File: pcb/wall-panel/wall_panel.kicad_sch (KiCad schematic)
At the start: 0 parts

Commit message: wall panel v0.3
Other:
- sheet CM4_HighSpeed ports: added BACKLIGHT_POWER; removed none
- sheet Power Filtering ports: added BACKLIGHT_POWER; removed none
- company: Grigorii Merkushev (aka brushknight) -> dotstar.tech
- title: Wall panel -> Wall Panel
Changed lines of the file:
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@@
 	(paper "A3")
 	(title_block
-		(title "Wall panel")
-		(date "2026-01-09")
-		(rev "1")
-		(company "Grigorii Merkushev (aka brushknight)")
-		(comment 1 "brushknight.com")
+		(title "Wall Panel")
+		(date "2026-02-02")
+		(rev "v0.3")
+		(company "dotstar.tech")
+		(comment 1 "designed by Grigorii Merkushev (aka brushknight)")
+		(comment 2 "brushknight.com")
 	)
 	(text "Connectors\n-------\nFAN\nBattery"
@@
 	(wire
 		(pts
+			(xy 168.91 87.63) (xy 203.2 87.63)
+		)
+		(stroke
+			(width 0)
+			(type default)
+		)
+	)
+	(wire
+		(pts
 			(xy 137.16 101.6) (xy 137.16 106.68)
 		)
@@
 	(wire
 		(pts
+			(xy 203.2 46.99) (xy 218.44 46.99)
+		)
+		(stroke
+			(width 0)
+			(type default)
+		)
+	)
+	(wire
+		(pts
 			(xy 168.91 135.89) (xy 179.07 135.89)
 		)
@@
 			(width 0)
 			(type solid)
+		)
+	)
+	(wire
+		(pts
+			(xy 203.2 87.63) (xy 203.2 46.99)
+		)
+		(stroke
+			(width 0)
+			(type default)
 		)
 	)
@@
 		(pin "TOUCH_SDA" input
 			(at 168.91 44.45 0)
+			(effects
+				(font
+					(size 1.27 1.27)
+				)
+				(justify right)
+			)
+		)
+		(pin "BACKLIGHT_POWER" input
+			(at 168.91 87.63 0)
 			(effects
 				(font
@@
 			(effects
 				(font
+					(size 1.27 1.27)
+				)
+				(justify left)
+			)
+		)
+		(pin "BACKLIGHT_POWER" output
+			(at 218.44 46.99 180)
+			(effects
+				(font

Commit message: small fixes of v0.3.1
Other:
- sheet CM4_GPIO ( Ethernet, GPIO, SDCARD) ports: added DISPLAY_PWM; removed none
- sheet CM4_HighSpeed ports: added DISPLAY_PWM; removed none
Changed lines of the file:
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@@
 	(title_block
 		(title "Wall Panel")
-		(date "2026-02-02")
-		(rev "v0.3")
+		(date "2026-02-25")
+		(rev "v0.3.1")
 		(company "dotstar.tech")
 		(comment 1 "designed by Grigorii Merkushev (aka brushknight)")
@@
 	(wire
 		(pts
+			(xy 180.34 128.27) (xy 180.34 90.17)
+		)
+		(stroke
+			(width 0)
+			(type default)
+		)
+	)
+	(wire
+		(pts
 			(xy 105.41 110.49) (xy 140.97 110.49)
 		)
@@
 	(wire
 		(pts
+			(xy 168.91 128.27) (xy 180.34 128.27)
+		)
+		(stroke
+			(width 0)
+			(type default)
+		)
+	)
+	(wire
+		(pts
 			(xy 105.41 106.68) (xy 137.16 106.68)
 		)
@@
 			(width 0)
 			(type solid)
+		)
+	)
+	(wire
+		(pts
+			(xy 180.34 90.17) (xy 168.91 90.17)
+		)
+		(stroke
+			(width 0)
+			(type default)
 		)
 	)
@@
 			)
 		)
+		(pin "DISPLAY_PWM" output
+			(at 168.91 128.27 0)
+			(effects
+				(font
+					(size 1.27 1.27)
+				)
+				(justify right)
+			)
+		)
 		(instances
 			(project "wall_panel"
@@
 			(effects
 				(font
+					(size 1.27 1.27)
+				)
+				(justify right)
+			)
+		)
+		(pin "DISPLAY_PWM" input
+			(at 168.91 90.17 0)
+			(effects
+				(font

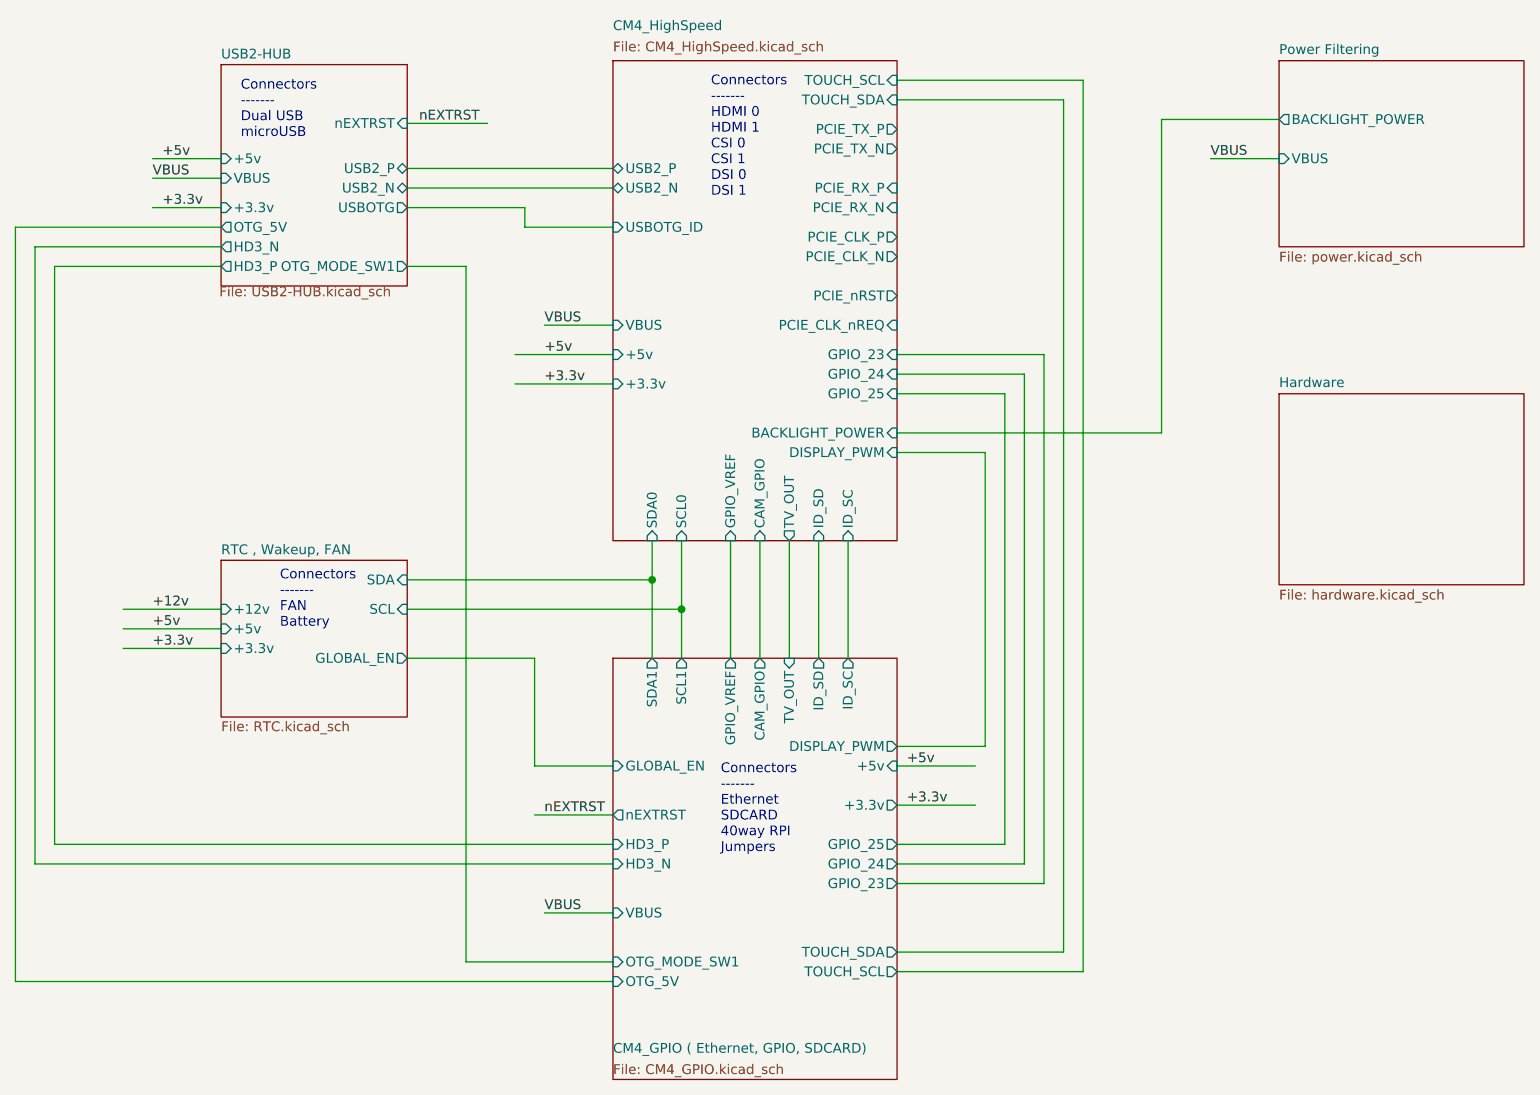
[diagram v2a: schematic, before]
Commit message: pogo pins wall panel
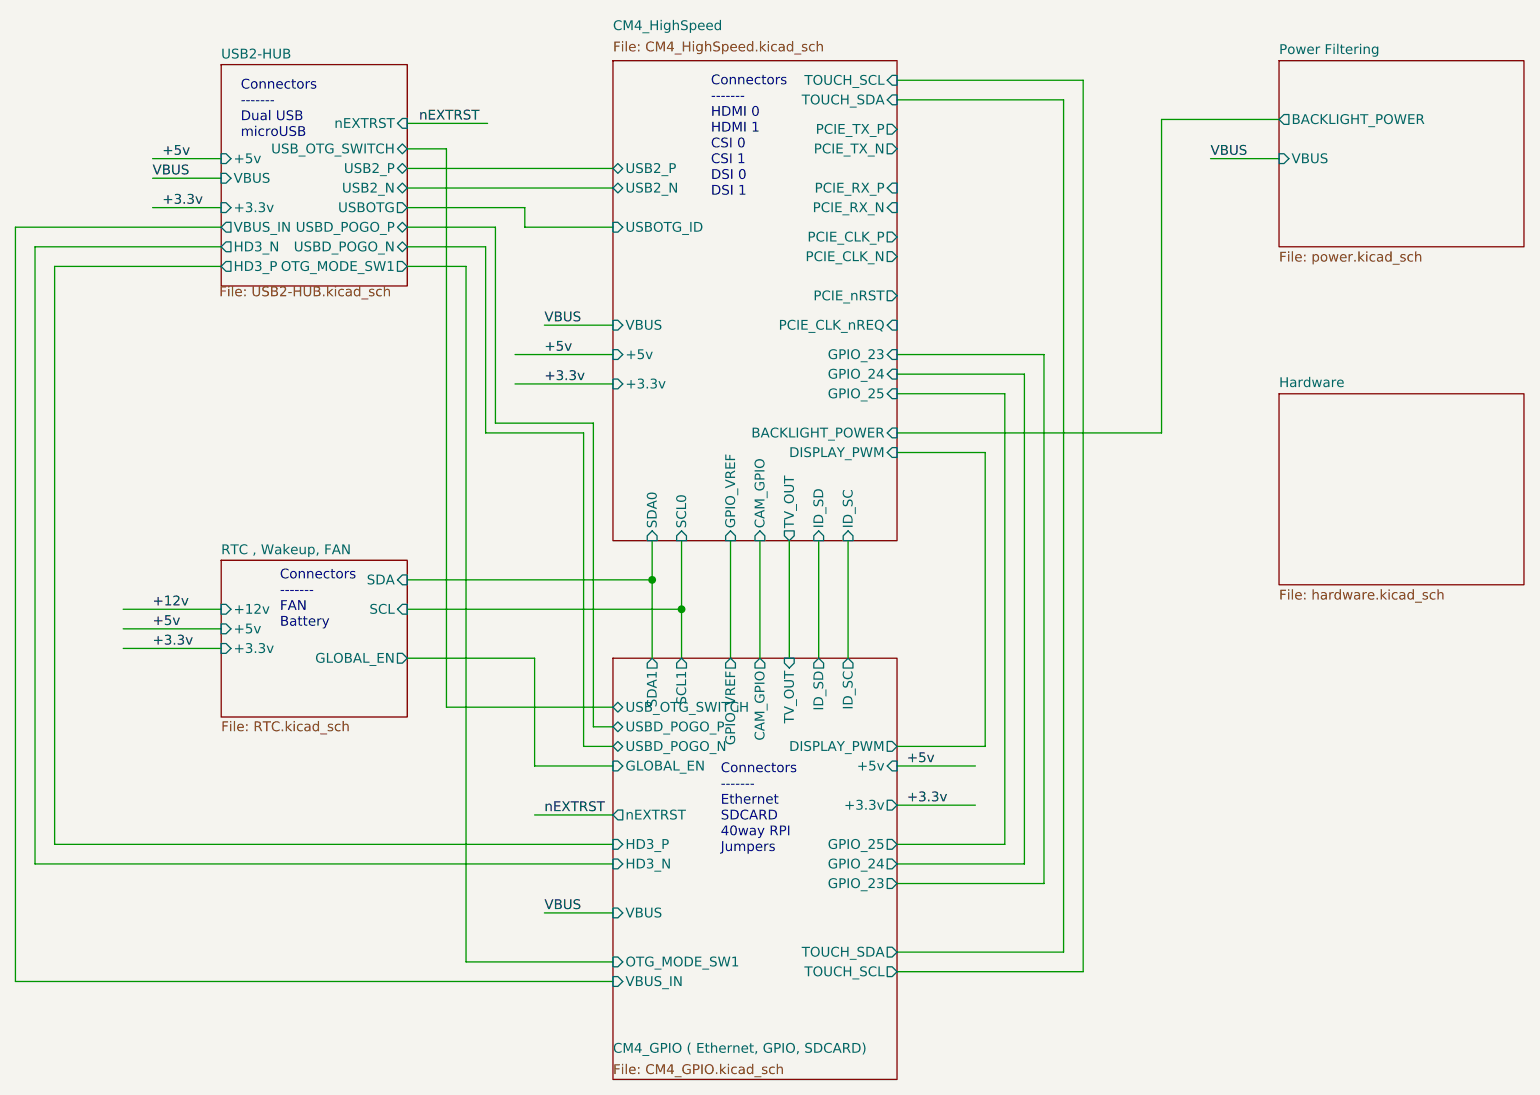
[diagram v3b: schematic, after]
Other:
- sheet CM4_GPIO ( Ethernet, GPIO, SDCARD) ports: added USBD_POGO_N, USBD_POGO_P, USB_OTG_SWITCH, VBUS_IN; removed OTG_5V
- sheet USB2-HUB ports: added USBD_POGO_N, USBD_POGO_P, USB_OTG_SWITCH, VBUS_IN; removed OTG_5V
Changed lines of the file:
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@@
 (kicad_sch
-	(version 20250114)
+	(version 20260306)
 	(generator "eeschema")
-	(generator_version "9.0")
+	(generator_version "10.0")
 	(paper "A3")
 	(title_block
@@
 	(wire
 		(pts
+			(xy 128.27 128.27) (xy 132.08 128.27)
+		)
+		(stroke
+			(width 0)
+			(type default)
+		)
+	)
+	(wire
+		(pts
 			(xy 168.91 143.51) (xy 185.42 143.51)
 		)
@@
 	(wire
 		(pts
+			(xy 129.54 125.73) (xy 129.54 86.36)
+		)
+		(stroke
+			(width 0)
+			(type default)
+		)
+	)
+	(wire
+		(pts
 			(xy 81.28 66.04) (xy 59.69 66.04)
 		)
@@
 	(wire
 		(pts
+			(xy 105.41 50.8) (xy 110.49 50.8)
+		)
+		(stroke
+			(width 0)
+			(type default)
+		)
+	)
+	(wire
+		(pts
 			(xy 147.32 101.6) (xy 147.32 116.84)
 		)
@@
 	(wire
 		(pts
+			(xy 105.41 63.5) (xy 115.57 63.5)
+		)
+		(stroke
+			(width 0)
+			(type default)
+		)
+	)
+	(wire
+		(pts
 			(xy 168.91 135.89) (xy 179.07 135.89)
 		)
@@
 	(wire
 		(pts
+			(xy 115.57 63.5) (xy 115.57 87.63)
+		)
+		(stroke
+			(width 0)
+			(type default)
+		)
+	)
+	(wire
+		(pts
+			(xy 128.27 87.63) (xy 128.27 128.27)
+		)
+		(stroke
+			(width 0)
+			(type default)
+		)
+	)
+	(wire
+		(pts
+			(xy 110.49 123.19) (xy 132.08 123.19)
+		)
+		(stroke
+			(width 0)
+			(type default)
+		)
+	)
+	(wire
+		(pts
+			(xy 110.49 50.8) (xy 110.49 123.19)
+		)
+		(stroke
+			(width 0)
+			(type default)
+		)
+	)
+	(wire
+		(pts
 			(xy 180.34 128.27) (xy 180.34 90.17)
 		)
@@
 	(wire
 		(pts
+			(xy 115.57 87.63) (xy 128.27 87.63)
+		)
+		(stroke
+			(width 0)
+			(type default)
+		)
+	)
+	(wire
+		(pts
 			(xy 203.2 87.63) (xy 203.2 46.99)
 		)
@@
 	(wire
 		(pts
+			(xy 116.84 86.36) (xy 116.84 60.96)
+		)
+		(stroke
+			(width 0)
+			(type default)
+		)
+	)
+	(wire
+		(pts
+			(xy 132.08 125.73) (xy 129.54 125.73)
+		)
+		(stroke
+			(width 0)
+			(type default)
+		)
+	)
+	(wire
+		(pts
 			(xy 132.08 143.51) (xy 57.15 143.51)
 		)
@@
 	(wire
 		(pts
+			(xy 129.54 86.36) (xy 116.84 86.36)
+		)
+		(stroke
+			(width 0)
+			(type default)
+		)
+	)
+	(wire
+		(pts
 			(xy 105.41 66.04) (xy 113.03 66.04)
 		)
@@
 		(pts
 			(xy 113.03 156.21) (xy 132.08 156.21)
+		)
+		(stroke
+			(width 0)
+			(type default)
+		)
+	)
+	(wire
+		(pts
+			(xy 116.84 60.96) (xy 105.41 60.96)
 		)
 		(stroke
@@
 		)
 		(fill
-			(color 255 255 255 0.0000)
+			(color 255 255 255 0)
 		)
 		(property "Sheetname" "CM4_GPIO ( Ethernet, GPIO, SDCARD)"
 			(at 132.08 168.148 0)
+			(show_name no)
+			(do_not_autoplace no)
 			(effects
 				(font
@@
 		(property "Sheetfile" "CM4_GPIO.kicad_sch"
 			(at 132.08 169.418 0)
+			(show_name no)
+			(do_not_autoplace no)
 			(effects
 				(font
@@
 			)
 		)
-		(pin "OTG_5V" input
+		(pin "VBUS_IN" input
 			(at 132.08 158.75 180)
 			(effects
@@
 				)
 				(justify right)
+			)
+		)
+		(pin "USBD_POGO_N" bidirectional
+			(at 132.08 128.27 180)
+			(effects
+				(font
+					(size 1.27 1.27)
+				)
+				(justify left)
+			)
+		)
+		(pin "USBD_POGO_P" bidirectional
+			(at 132.08 125.73 180)
+			(effects
+				(font
+					(size 1.27 1.27)
+				)
+				(justify left)
+			)
+		)
+		(pin "USB_OTG_SWITCH" bidirectional
+			(at 132.08 123.19 180)
+			(effects
+				(font
+					(size 1.27 1.27)
+				)
+				(justify left)
 			)
 		)
@@
 		)
 		(fill
-			(color 255 255 255 0.0000)
+			(color 255 255 255 0)
 		)
 		(property "Sheetname" "CM4_HighSpeed"
 			(at 132.08 35.56 0)
+			(show_name no)
+			(do_not_autoplace no)
 			(effects
 				(font
@@
 		(property "Sheetfile" "CM4_HighSpeed.kicad_sch"
 			(at 132.08 36.83 0)
+			(show_name no)
+			(do_not_autoplace no)
 			(effects
 				(font
@@
 		)
 		(fill
-			(color 255 255 255 0.0000)
+			(color 255 255 255 0)
 		)
 		(property "Sheetname" "USB2-HUB"
 			(at 81.28 39.2425 0)
+			(show_name no)
+			(do_not_autoplace no)
 			(effects
 				(font
@@
 		(property "Sheetfile" "USB2-HUB.kicad_sch"
 			(at 81.026 68.58 0)
+			(show_name no)
+			(do_not_autoplace no)
 			(effects
 				(font
@@
 			)
 		)
-		(pin "OTG_5V" output
+		(pin "VBUS_IN" output
 			(at 81.28 60.96 180)
 			(effects
@@
 				)
 				(justify left)
+			)
+		)
+		(pin "USBD_POGO_P" bidirectional
+			(at 105.41 60.96 0)
+			(effects
+				(font
+					(size 1.27 1.27)
+				)
+				(justify right)
+			)
+		)
+		(pin "USBD_POGO_N" bidirectional
+			(at 105.41 63.5 0)
+			(effects
+				(font
+					(size 1.27 1.27)
+				)
+				(justify right)
+			)
+		)
+		(pin "USB_OTG_SWITCH" bidirectional
+			(at 105.41 50.8 0)
+			(effects
+				(font
+					(size 1.27 1.27)
+				)
+				(justify right)
 			)
 		)
@@
 		)
 		(fill
-			(color 255 255 255 0.0000)
+			(color 255 255 255 0)
 		)
 		(property "Sheetname" "RTC , Wakeup, FAN"
 			(at 81.28 103.5045 0)
+			(show_name no)
+			(do_not_autoplace no)
 			(effects
 				(font
@@
 		(property "Sheetfile" "RTC.kicad_sch"
 			(at 81.28 124.9685 0)
+			(show_name no)
+			(do_not_autoplace no)
 			(effects
 				(font
@@
 		)
 		(fill
-			(color 0 0 0 0.0000)
+			(color 0 0 0 0)
 		)
 		(property "Sheetname" "Hardware"
 			(at 218.44 81.8384 0)
+			(show_name no)
+			(do_not_autoplace no)
 			(effects
 				(font
@@
 		(property "Sheetfile" "hardware.kicad_sch"
 			(at 218.44 107.8996 0)
+			(show_name no)
+			(do_not_autoplace no)
 			(effects
 				(font
@@
 		)
 		(fill
-			(color 0 0 0 0.0000)
+			(color 0 0 0 0)
 		)
 		(property "Sheetname" "Power Filtering"
 			(at 218.44 38.6584 0)
+			(show_name no)
+			(do_not_autoplace no)
 			(effects
 				(font
@@
 		(property "Sheetfile" "power.kicad_sch"
 			(at 218.44 64.0846 0)
-			(effects
-				(font
+			(show_name no)
+			(do_not_autoplace no)
+			(effects
+				(font
